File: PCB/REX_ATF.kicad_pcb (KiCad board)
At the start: 2 copper layers, 38 x 16.6 mm, 9 parts, among them J1 Tandy_100_102_200_option_rom, J2 JTAG, U1 ATF1504ASL-xAx44, U2 29F800BB

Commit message: move some traces around
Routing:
- net VBUS: track 65.5 -> 62.9 mm, vias 8 -> 6
- net /A10: track 7.15 -> 6.07 mm, vias 1 -> 0
- net /ad6: track 10.9 -> 11.9 mm
- net /ad5: track 11.7 -> 12.3 mm
- net /TP1: track 17.9 -> 18.0 mm, vias 1 -> 0
- net /TP2: vias 1 -> 0
- net GND: vias 56 -> 53

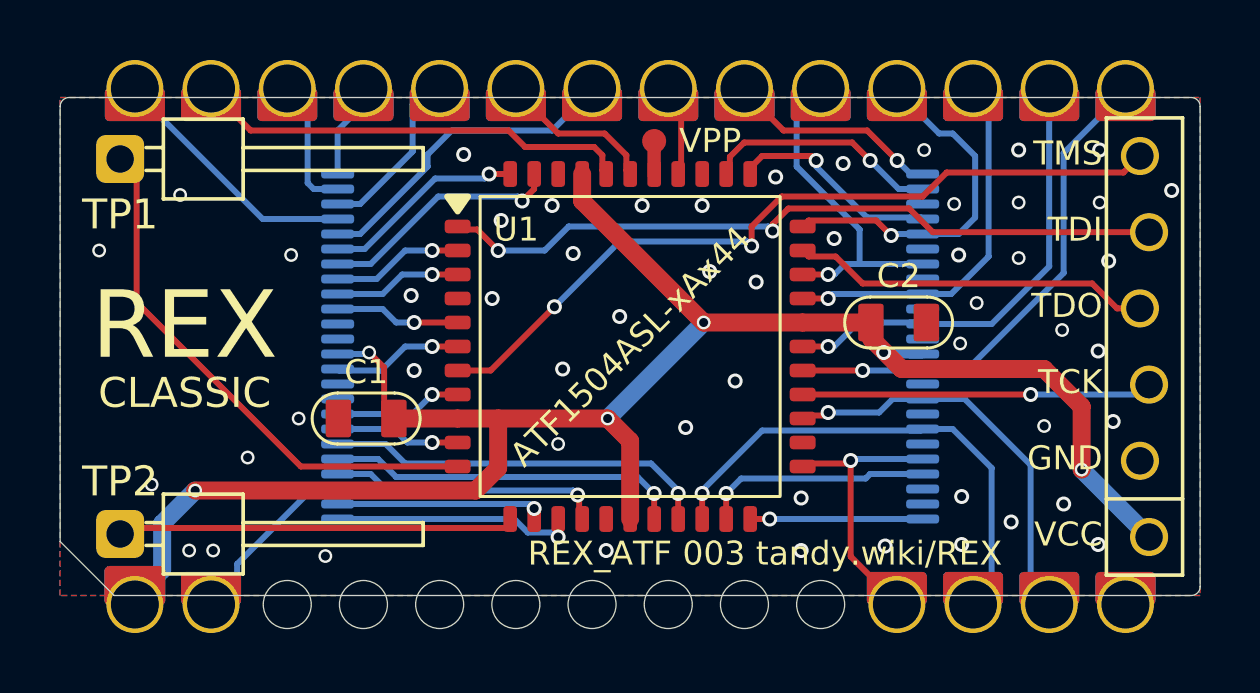
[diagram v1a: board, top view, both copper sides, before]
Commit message: use nc pins for pcb ground path
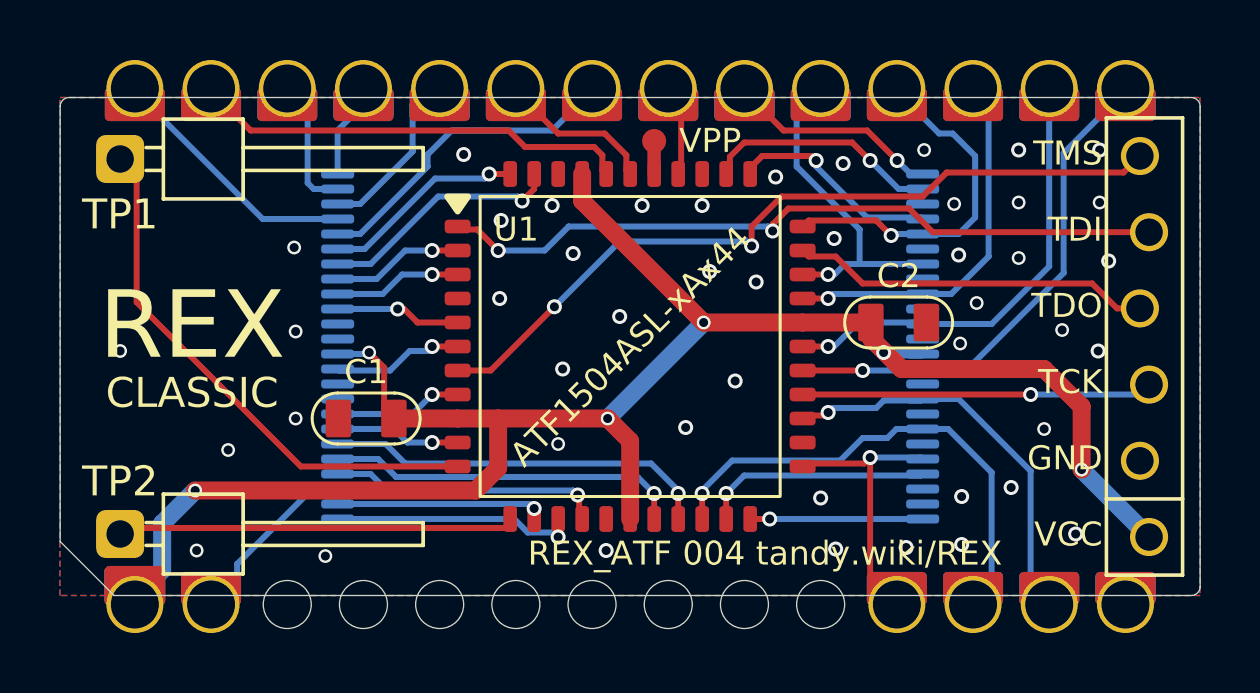
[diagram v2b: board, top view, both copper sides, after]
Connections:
- U2 pad 10: unconnected-(U2-NC-Pad10) -> GND
- U2 pad 13: unconnected-(U2-NC-Pad13) -> GND
- U2 pad 14: unconnected-(U2-NC-Pad14) -> GND
- U2 pad 9: unconnected-(U2-NC(A19)-Pad9) -> GND
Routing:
- net GND: vias 53 -> 46

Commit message: move ALE to a GCLK pin and init /CSA & /CSB high
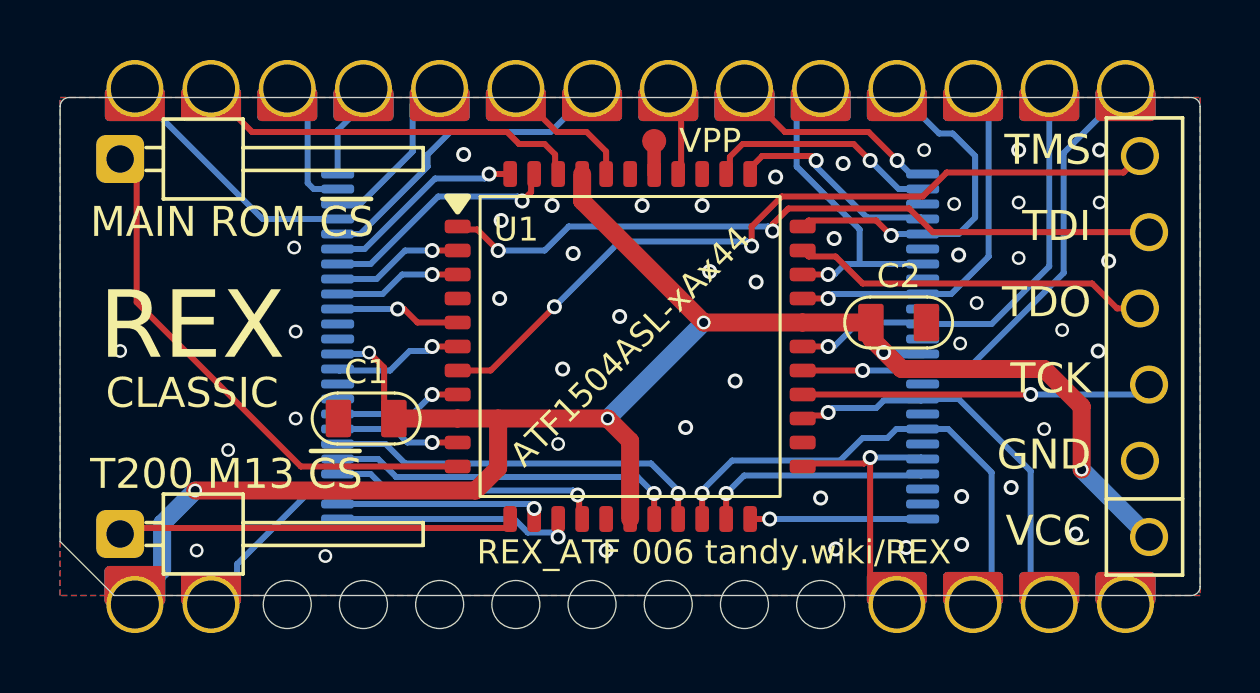
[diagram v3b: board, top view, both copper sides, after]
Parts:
- TP1: value cs_MAIN1 -> MAIN ROM ~{CS}
- TP2: value cs_MAIN2A -> T200 M13 ~{CS}
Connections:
- net /RY/~{BY} renamed /~{BY}mem
- net /TP1 renamed /~{CSA}
- net /TP2 renamed /~{CSB}
- net /~{CE_FLASH} renamed /~{CE}mem
- net /~{OE_BUS} renamed /~{OE}
- net /~{OE_FLASH} renamed /~{OE}mem
- net /~{WE_FLASH} renamed /~{WE}mem
- J1 pad 23: /ALE_BUS -> /ALE
- J1 pad 27: /~{CS_BUS} -> /~{CS}
- U1 pad 39: /ALE_BUS -> unconnected-(U1-I/GCLR-Pad39)
- U1 pad 40: /~{CS_BUS} -> /ALE
- U1 pad 42: unconnected-(U1-A16-Pad42) -> /~{CS}
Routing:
- net /~{CS_BUS}: track 14.4 -> 0.00 mm
- net /~{CS}: track 0.00 -> 12.9 mm
- net /ALE_BUS: track 5.06 -> 0.00 mm
- net /ALE: track 0.00 -> 4.41 mm

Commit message: external pullups on CSA CSB
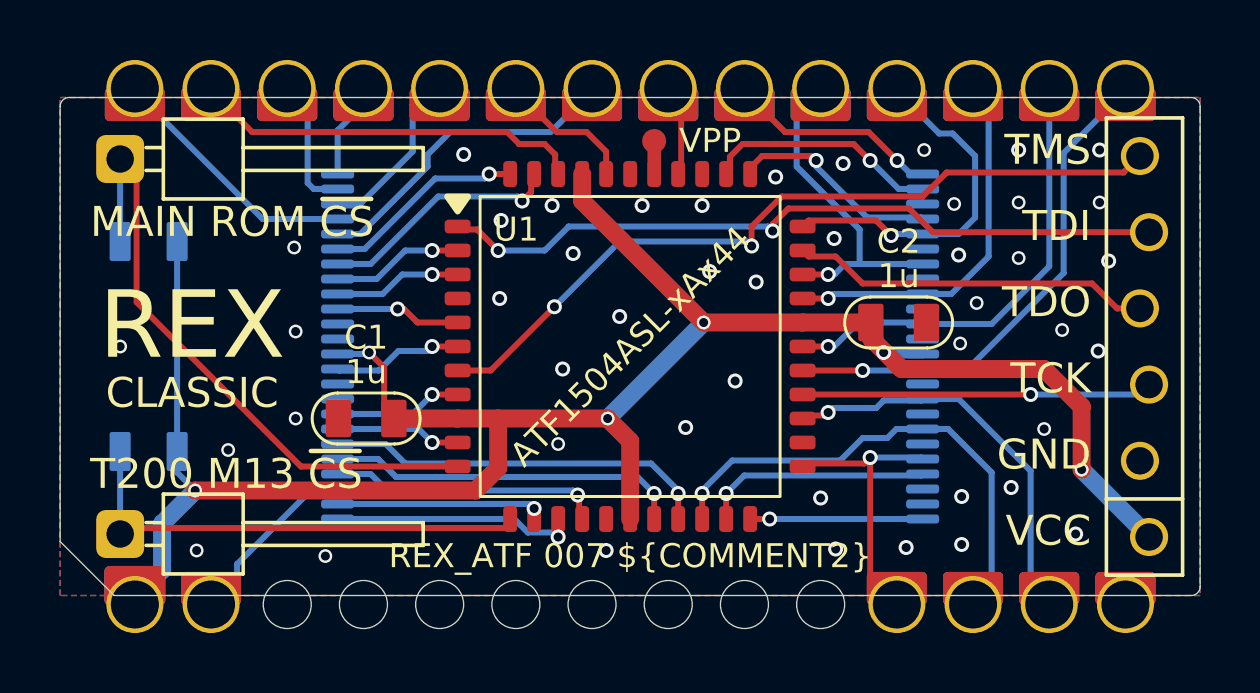
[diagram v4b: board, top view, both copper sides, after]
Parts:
- added R1: 47K, 000_LOCAL:R_0805, B.Cu at (121.2, 95.7)
- added R2: 47K, 000_LOCAL:R_0805, B.Cu at (121.2, 102.7)
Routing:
- net VBUS: track 62.9 -> 71.5 mm
- net /~{CSB}: track 13.4 -> 16.1 mm
- net /~{CSA}: track 18.0 -> 20.7 mm
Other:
- board text added: "${COMMENT1}"
- board text added: "Carrier: shpws.me/SGGB"
- board text removed: "C*: ${00000000-0000-0000-0000-00005d17005c:VALUE} shpws.me/SGGB"

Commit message: enable pin keeper option
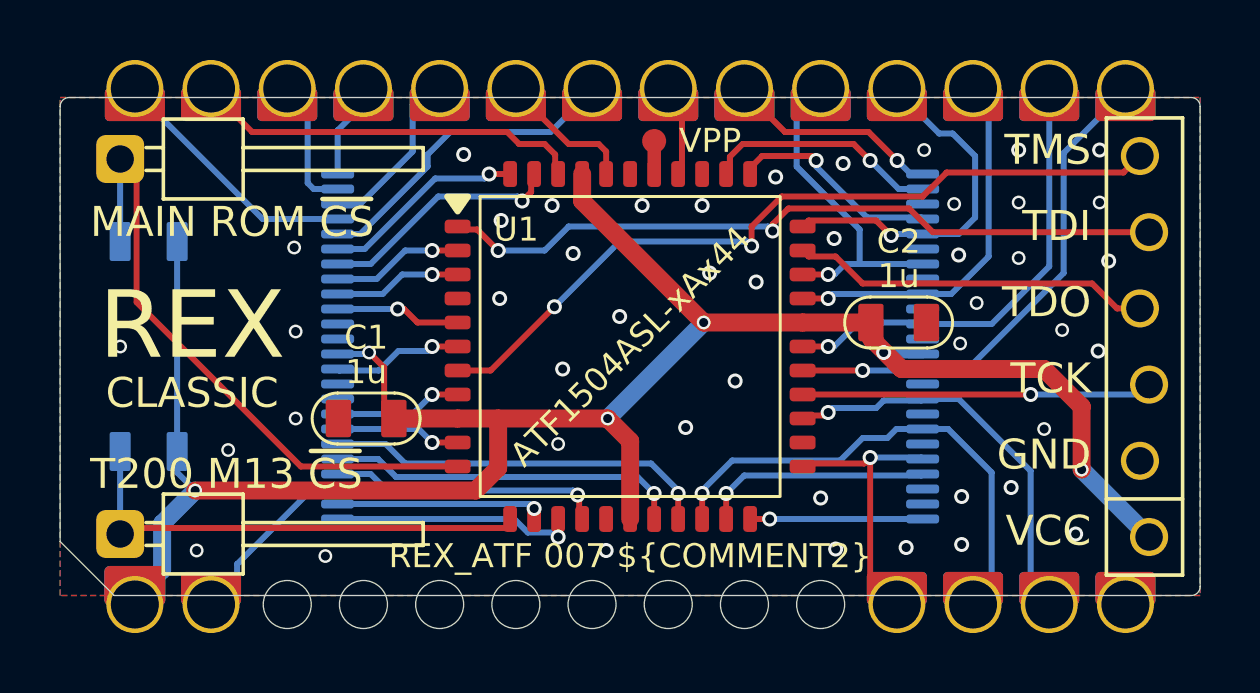
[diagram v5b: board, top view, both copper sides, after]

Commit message: minor pcb touches, update readme
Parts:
- added N1: Housing, 000_LOCAL:Housing_Molex78802_PCB_28, F.Cu at (137.2, 99.2)
- J1: value Tandy_100_102_200_option_rom -> Tandy_100_102_200_option_rom socket edge connections
- TP1: value MAIN ROM ~{CS} -> MAIN_ROM_~{CS}
- TP2: value T200 M13 ~{CS} -> T200_M13_~{CS}
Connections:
- U1 pad 42: /~{CS} -> /~{BY}mem
- U1 pad 5: /~{BY}mem -> /~{CS}
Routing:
- net /~{BY}mem: track 4.19 -> 10.9 mm
- net VBUS: track 71.5 -> 74.8 mm, vias 6 -> 10
- net /~{CS}: track 12.9 -> 14.3 mm
- net GND: vias 46 -> 64
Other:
- board text removed: "Carrier: shpws.me/SGGB"
